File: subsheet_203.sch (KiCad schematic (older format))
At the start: 14 parts, among them U203 MC68901_DIP_48_PHY, U209 74LS86_PHY, U211 74LS04_PHY, U900 74LS164_PHY, Y200 2.4576 MHz

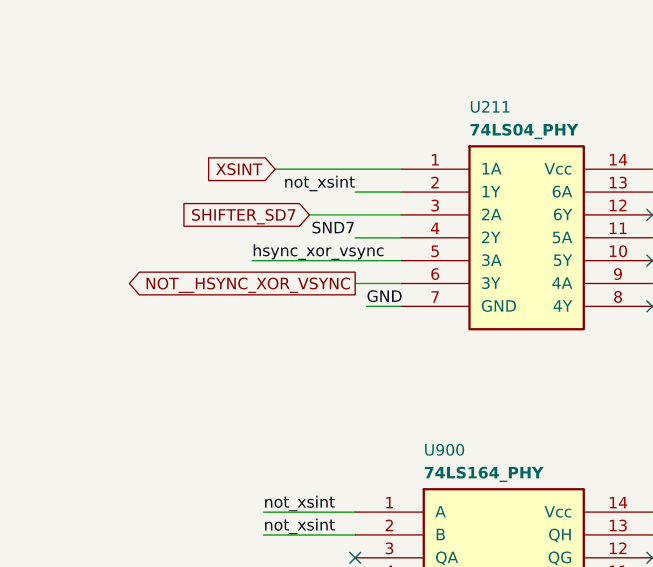
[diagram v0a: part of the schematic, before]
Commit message: Delete circuitry related to PAL/NTSC and modulator
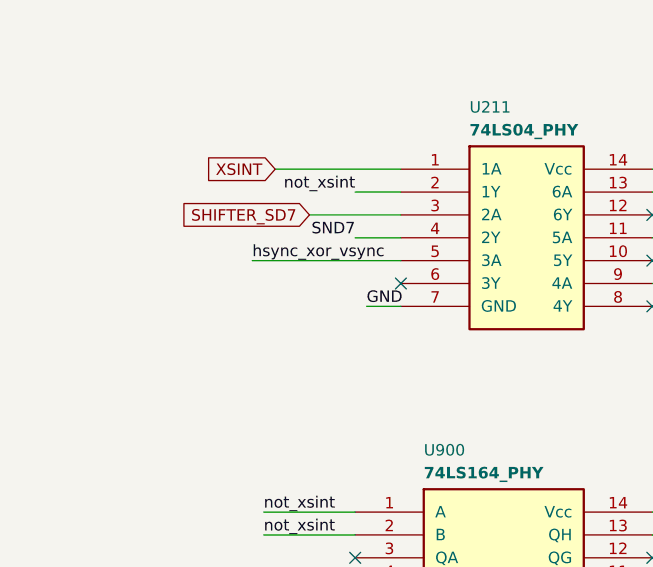
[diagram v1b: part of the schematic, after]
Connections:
- net NOT__HSYNC_XOR_VSYNC: no longer names the net of U211.6 (3Y)
- no-connect marks 19 -> 20
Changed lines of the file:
@@
 Text Label 1850 7200 0    50   ~ 0
 hsync_xor_vsync
-Text GLabel 2300 7300 0    50   Output ~ 0
-NOT__HSYNC_XOR_VSYNC
-Wire Wire Line
-	2300 7300 2500 7300
 Text Label 2350 7400 0    50   ~ 0
 GND
@@
 Wire Wire Line
 	6750 2150 6750 2350
+NoConn ~ 2500 7300
 $EndSCHEMATC

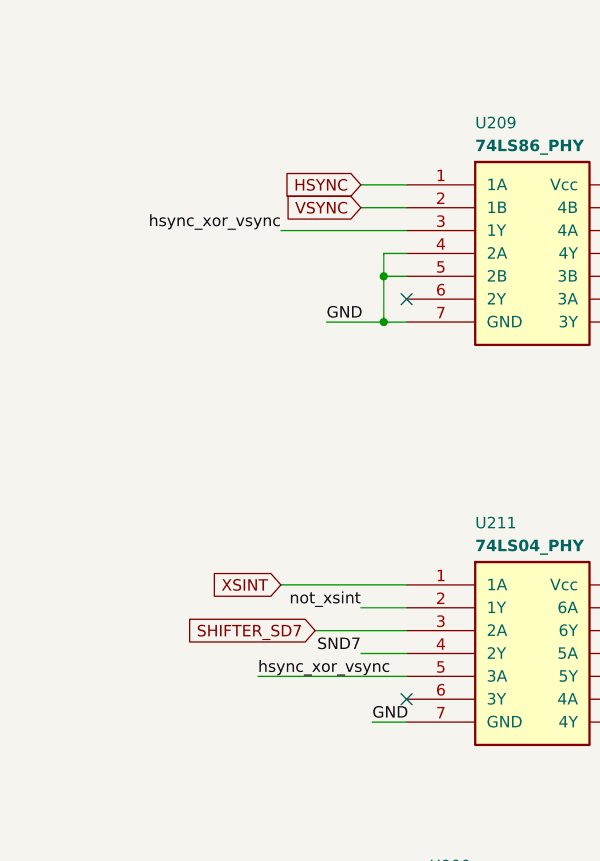
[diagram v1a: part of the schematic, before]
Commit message: Removed T-filters
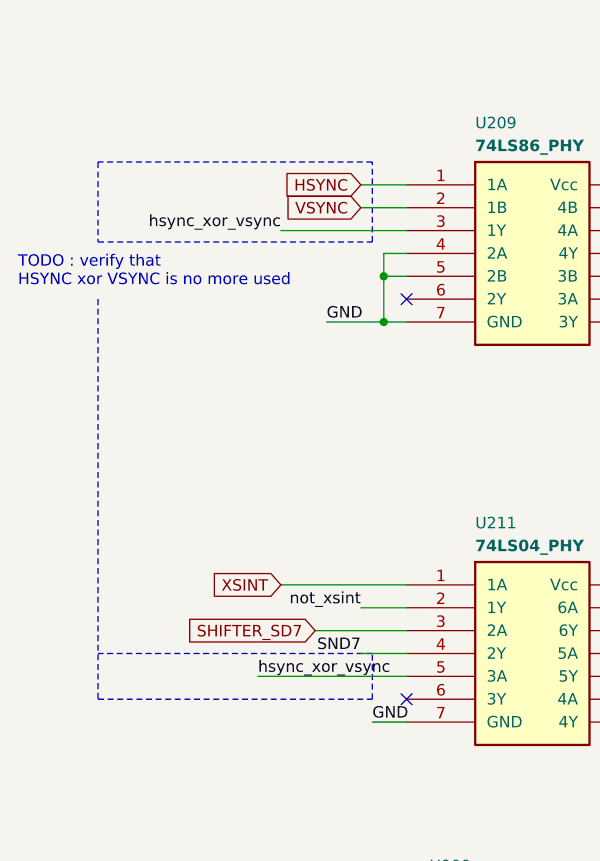
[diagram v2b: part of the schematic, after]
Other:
- note added: "TODO : verify that\nHSYNC xor VSYNC is no more used"
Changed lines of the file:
@@
 	6750 2150 6750 2350
 NoConn ~ 2500 7300
+Text Notes 800  5500 0    50   ~ 0
+TODO : verify that\nHSYNC xor VSYNC is no more used
+Wire Notes Line
+	2350 4950 1150 4950
+Wire Notes Line
+	1150 4950 1150 5300
+Wire Notes Line
+	1150 5300 2350 5300
+Wire Notes Line
+	2350 5300 2350 4950
+Wire Notes Line
+	1150 5550 1150 7300
+Wire Notes Line
+	1150 7300 2350 7300
+Wire Notes Line
+	2350 7300 2350 7100
+Wire Notes Line
+	2350 7100 1150 7100
 $EndSCHEMATC

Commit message: Resolves #13 : assign 1206 hand-solder footprints to resistors
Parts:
- R215, R216, R217: footprint commons_passives_THT:Passive_THT_resistor_W2.54mm_L12.70mm -> Resistor_SMD:R_1206_3216Metric_Pad1.30x1.75mm_HandSolder
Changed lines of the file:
@@
 F 0 "R217" V 6150 3250 50  0000 C CNN
 F 1 "4K7" V 6350 3250 50  0000 C CNN
-F 2 "commons_passives_THT:Passive_THT_resistor_W2.54mm_L12.70mm" H 6250 3250 50  0001 C CNN
+F 2 "Resistor_SMD:R_1206_3216Metric_Pad1.30x1.75mm_HandSolder" H 6250 3250 50  0001 C CNN
 F 3 "~" H 6250 3250 50  0001 C CNN
 	1    6250 3250
@@
 F 0 "R215" V 6150 2750 50  0000 C CNN
 F 1 "4K7" V 6350 2750 50  0000 C CNN
-F 2 "commons_passives_THT:Passive_THT_resistor_W2.54mm_L12.70mm" H 6250 2750 50  0001 C CNN
+F 2 "Resistor_SMD:R_1206_3216Metric_Pad1.30x1.75mm_HandSolder" H 6250 2750 50  0001 C CNN
 F 3 "~" H 6250 2750 50  0001 C CNN
 	1    6250 2750
@@
 F 0 "R216" V 6150 3750 50  0000 C CNN
 F 1 "4K7" V 6350 3750 50  0000 C CNN
-F 2 "commons_passives_THT:Passive_THT_resistor_W2.54mm_L12.70mm" H 6250 3750 50  0001 C CNN
+F 2 "Resistor_SMD:R_1206_3216Metric_Pad1.30x1.75mm_HandSolder" H 6250 3750 50  0001 C CNN
 F 3 "~" H 6250 3750 50  0001 C CNN
 	1    6250 3750

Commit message: Resolves #8 : Assign 1206 hand-solder footprints to non polarized capacitors
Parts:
- C219, C220: footprint commons_passives_THT:Passive_THT_capacitor_W2.54mm_L10.16mm -> Capacitor_SMD:C_1206_3216Metric_Pad1.33x1.80mm_HandSolder
- C221, C229, C230, C900: footprint commons_passives_THT:Passive_THT_capacitor_mlcc_W2.54mm_L7.62mm -> Capacitor_SMD:C_1206_3216Metric_Pad1.33x1.80mm_HandSolder
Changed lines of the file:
@@
 F 0 "C900" H 4575 8650 50  0000 L CNN
 F 1 "0.1uF" H 4575 8450 50  0000 L CNN
-F 2 "commons_passives_THT:Passive_THT_capacitor_mlcc_W2.54mm_L7.62mm" H 4588 8400 50  0001 C CNN
+F 2 "Capacitor_SMD:C_1206_3216Metric_Pad1.33x1.80mm_HandSolder" H 4588 8400 50  0001 C CNN
 F 3 "~" H 4550 8550 50  0001 C CNN
 	1    4550 8550
@@
 F 0 "C230" H 4275 7200 50  0000 L CNN
 F 1 "0.1uF" H 4275 7000 50  0000 L CNN
-F 2 "commons_passives_THT:Passive_THT_capacitor_mlcc_W2.54mm_L7.62mm" H 4288 6950 50  0001 C CNN
+F 2 "Capacitor_SMD:C_1206_3216Metric_Pad1.33x1.80mm_HandSolder" H 4288 6950 50  0001 C CNN
 F 3 "~" H 4250 7100 50  0001 C CNN
 	1    4250 7100
@@
 F 0 "C229" H 5275 5400 50  0000 L CNN
 F 1 "0.1uF" H 5275 5200 50  0000 L CNN
-F 2 "commons_passives_THT:Passive_THT_capacitor_mlcc_W2.54mm_L7.62mm" H 5288 5150 50  0001 C CNN
+F 2 "Capacitor_SMD:C_1206_3216Metric_Pad1.33x1.80mm_HandSolder" H 5288 5150 50  0001 C CNN
 F 3 "~" H 5250 5300 50  0001 C CNN
 	1    5250 5300
@@
 F 0 "C221" H 1025 3200 50  0000 L CNN
 F 1 "0.1uF" H 1025 3000 50  0000 L CNN
-F 2 "commons_passives_THT:Passive_THT_capacitor_mlcc_W2.54mm_L7.62mm" H 1038 2950 50  0001 C CNN
+F 2 "Capacitor_SMD:C_1206_3216Metric_Pad1.33x1.80mm_HandSolder" H 1038 2950 50  0001 C CNN
 F 3 "~" H 1000 3100 50  0001 C CNN
 	1    1000 3100
@@
 F 0 "C219" H 5775 2100 50  0000 L CNN
 F 1 "30pF" H 5775 1900 50  0000 L CNN
-F 2 "commons_passives_THT:Passive_THT_capacitor_W2.54mm_L10.16mm" H 5788 1850 50  0001 C CNN
+F 2 "Capacitor_SMD:C_1206_3216Metric_Pad1.33x1.80mm_HandSolder" H 5788 1850 50  0001 C CNN
 F 3 "~" H 5750 2000 50  0001 C CNN
 	1    5750 2000
@@
 F 0 "C220" H 6775 2100 50  0000 L CNN
 F 1 "30pF" H 6775 1900 50  0000 L CNN
-F 2 "commons_passives_THT:Passive_THT_capacitor_W2.54mm_L10.16mm" H 6788 1850 50  0001 C CNN
+F 2 "Capacitor_SMD:C_1206_3216Metric_Pad1.33x1.80mm_HandSolder" H 6788 1850 50  0001 C CNN
 F 3 "~" H 6750 2000 50  0001 C CNN
 	1    6750 2000
